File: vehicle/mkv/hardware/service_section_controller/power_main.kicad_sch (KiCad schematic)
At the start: 32 parts

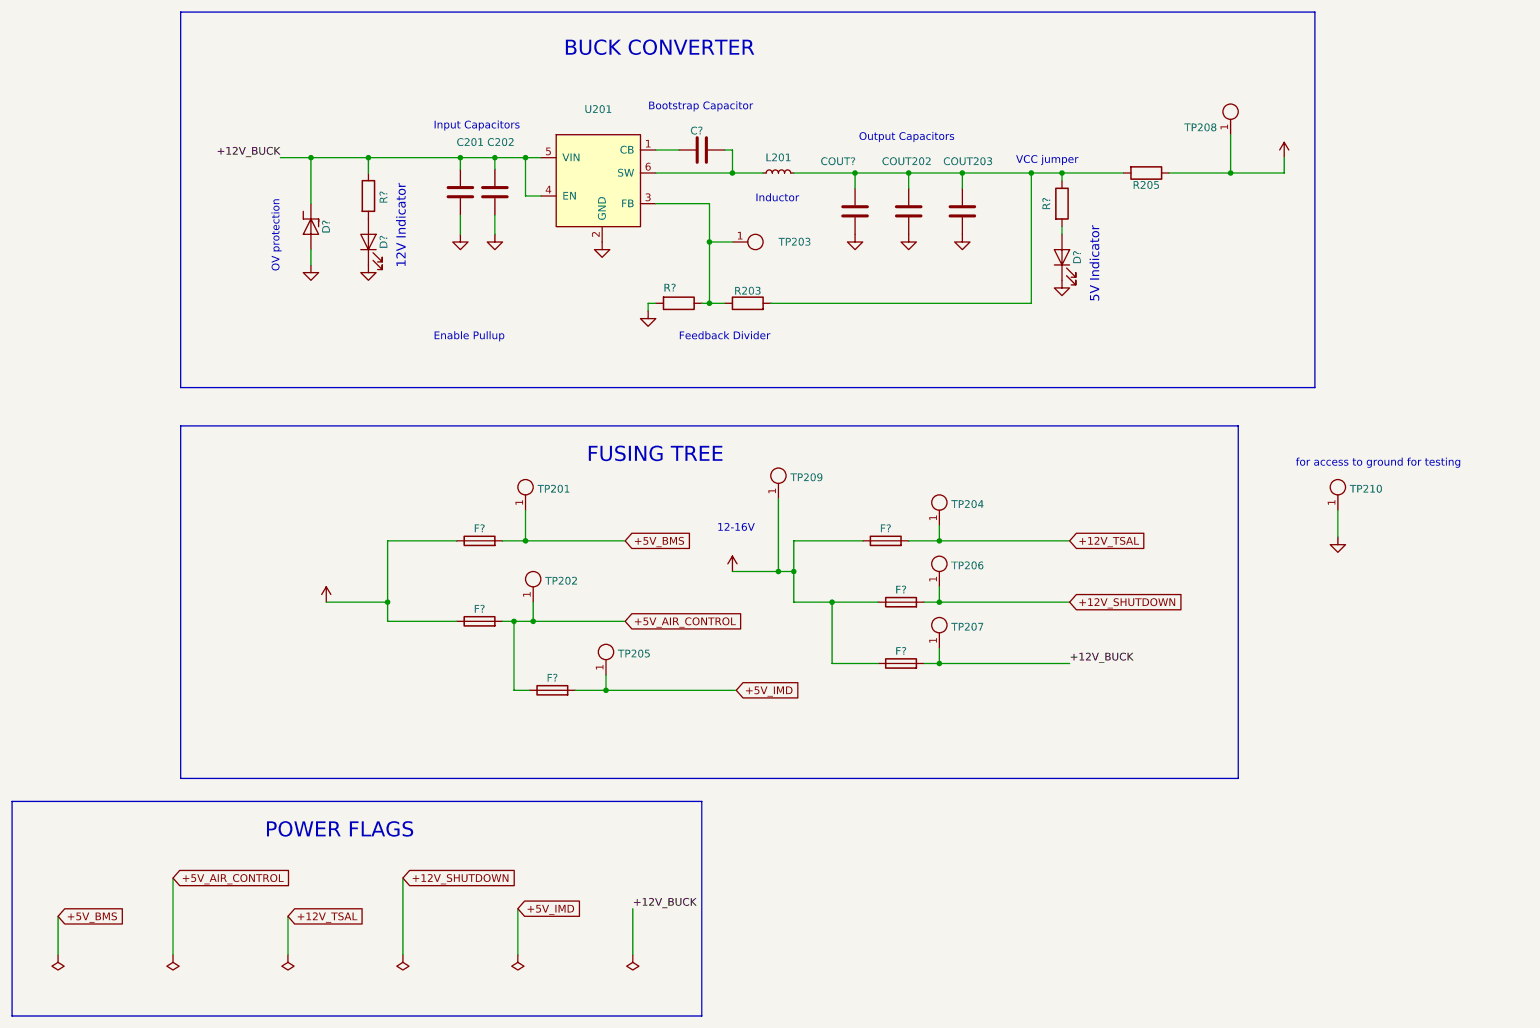
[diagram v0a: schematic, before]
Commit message: chore: annotate migrated schematics
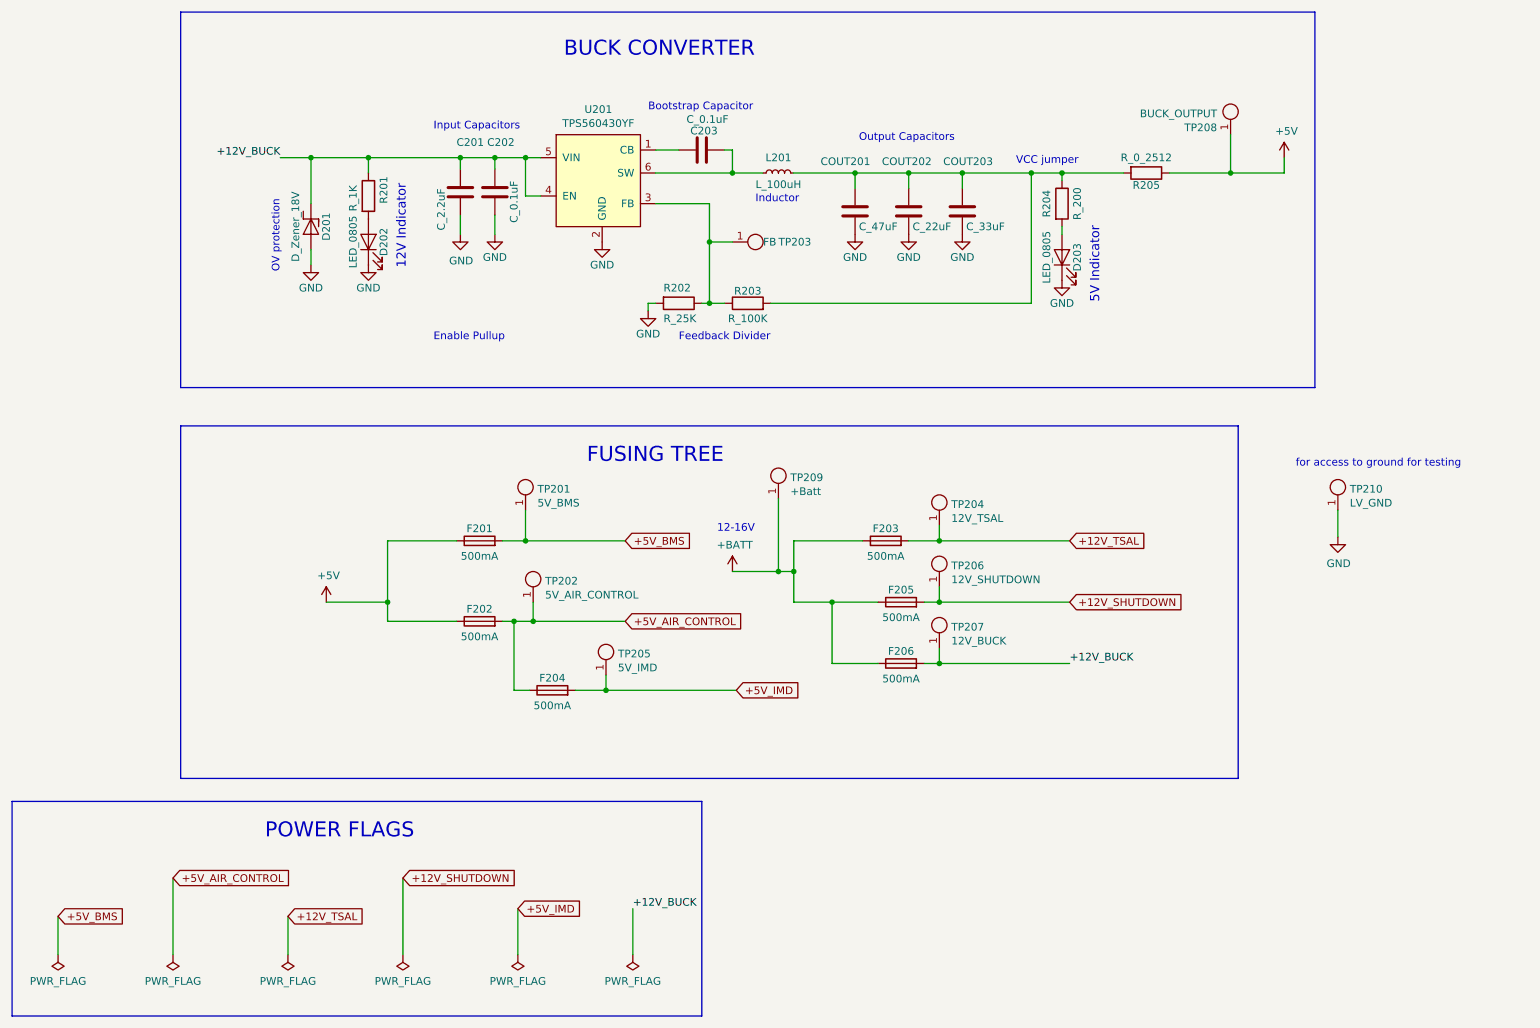
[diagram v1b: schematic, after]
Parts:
- C201: value (none) -> C_2.2uF; footprint (none) -> footprints:C_0603_1608Metric
- C202: value (none) -> C_0.1uF; footprint (none) -> footprints:C_0805_OEM
- C203: renamed from C?; value (none) -> C_0.1uF; footprint (none) -> footprints:C_0805_OEM
- COUT201: renamed from COUT?; value (none) -> C_47uF; footprint (none) -> footprints:C_0805_OEM
- COUT202: value (none) -> C_22uF; footprint (none) -> footprints:C_1206_OEM
- COUT203: value (none) -> C_33uF; footprint (none) -> footprints:Fuse_1812
- D201: renamed from D?; value (none) -> D_Zener_18V; footprint (none) -> footprints:DO-214AA
- D202, D203: renamed from D?; value (none) -> LED_0805; footprint (none) -> footprints:LED_0805_OEM
- F201, F202, F203, F204, F205, F206: renamed from F?; value (none) -> 500mA; footprint (none) -> footprints:Fuse_1210
- L201: value (none) -> L_100uH; footprint (none) -> footprints:L_100uH_OEM
- R201: renamed from R?; value (none) -> R_1K; footprint (none) -> footprints:R_0805_OEM
- R202: renamed from R?; value (none) -> R_25K; footprint (none) -> footprints:R_0805_OEM
- R203: value (none) -> R_100K; footprint (none) -> footprints:R_0805_OEM
- R204: renamed from R?; value (none) -> R_200; footprint (none) -> footprints:R_0805_OEM
- R205: value (none) -> R_0_2512; footprint (none) -> footprints:R_2512_OEM
- TP201: value (none) -> 5V_BMS; footprint (none) -> TestPoint:TestPoint_Pad_D1.0mm
- TP202: value (none) -> 5V_AIR_CONTROL; footprint (none) -> TestPoint:TestPoint_Pad_D1.0mm
- TP203: value (none) -> FB; footprint (none) -> TestPoint:TestPoint_Pad_D1.0mm
- TP204: value (none) -> 12V_TSAL; footprint (none) -> TestPoint:TestPoint_Pad_D1.0mm
- TP205: value (none) -> 5V_IMD; footprint (none) -> TestPoint:TestPoint_Pad_D1.0mm
- TP206: value (none) -> 12V_SHUTDOWN; footprint (none) -> TestPoint:TestPoint_Pad_D1.0mm
- TP207: value (none) -> 12V_BUCK; footprint (none) -> TestPoint:TestPoint_Pad_D1.0mm
- TP208: value (none) -> BUCK_OUTPUT; footprint (none) -> TestPoint:TestPoint_Pad_D4.0mm
- TP209: value (none) -> +Batt; footprint (none) -> TestPoint:TestPoint_Pad_D4.0mm
- TP210: value (none) -> LV_GND; footprint (none) -> TestPoint:TestPoint_Pad_D4.0mm
- U201: value (none) -> TPS560430YF; footprint (none) -> footprints:SOT-23-6_OEM
